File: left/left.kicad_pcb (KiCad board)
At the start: 2 copper layers, 143.8 x 147.7 mm, 47 parts, among them J1 USB_C_Receptacle_USB2.0, J2 Conn_01x04, J3 Conn_01x06, SW1 SW_Push, SW10 SW_Push, SW11 SW_Push, SW12 SW_Push, SW13 SW_Push, SW14 SW_Push, SW15 SW_Push, SW16 SW_Push, SW17 SW_Push, SW18 SW_Push, SW19 SW_Push, SW2 SW_Push, SW20 SW_Push, SW21 SW_Push, SW22 SW_Push, SW23 SW_Push, SW24 SW_Push, SW25 SW_Push, SW26 SW_Push, SW27 SW_Push, SW28 SW_Push, SW29 SW_Push, SW3 RotaryEncoder_Switch, SW30 SW_Push, SW31 SW_Push, SW32 SW_Push, SW33 SW_Push, SW34 SW_Push, SW4 SW_Push, SW5 SW_Push, SW6 SW_Push, SW7 SW_Push, SW8 SW_Push, SW9 SW_Push, U1 HOLYIOT-18010-NRF52840

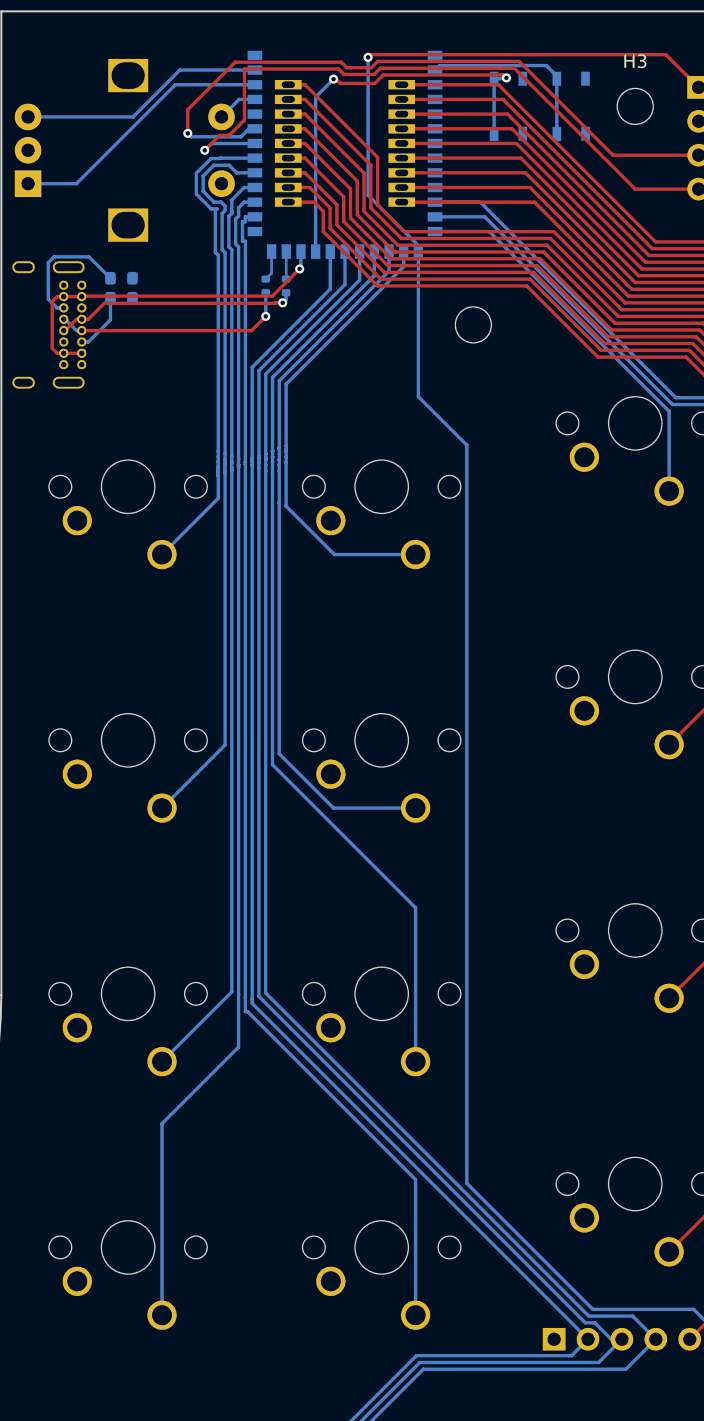
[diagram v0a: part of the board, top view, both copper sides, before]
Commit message: update footprint of rf module
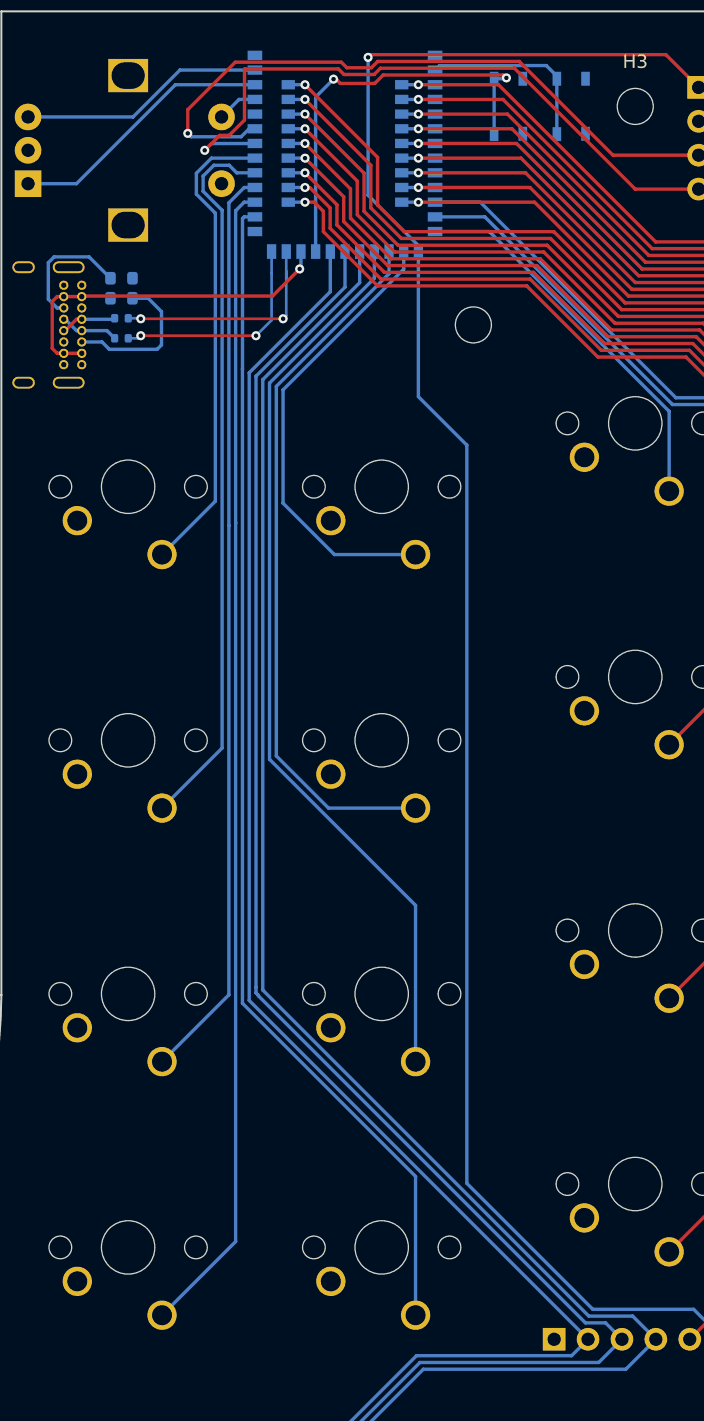
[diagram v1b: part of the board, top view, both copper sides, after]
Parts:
- moved R3 12.6 mm to (88.9, 42.0), turned to 0 degrees
- moved R4 11.5 mm to (88.9, 43.5), turned to 0 degrees
- moved BT1 7.15 mm to (190.8, 25.5)
- turned R2 to 0 degrees
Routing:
- net D-: track 2.07 -> 17.3 mm, vias 0 -> 2
- net D+: track 2.25 -> 16.4 mm, vias 0 -> 2
- net Net-(J1-PadA7): track 18.1 -> 4.20 mm, vias 1 -> 0
- net Net-(J1-PadA6): track 17.7 -> 4.41 mm, vias 1 -> 0
- net Net-(J1-PadA5): track 4.46 -> 11.4 mm
- net S10: track 55.0 -> 54.3 mm
- net S00: track 36.3 -> 35.7 mm
- net S35: vias 0 -> 1
- net S05: vias 0 -> 1
- net S60: vias 0 -> 1
- net S45: vias 0 -> 1
- net S44: vias 0 -> 1
- net S43: vias 0 -> 1
- net S42: vias 0 -> 1
- net S34: vias 0 -> 1
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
